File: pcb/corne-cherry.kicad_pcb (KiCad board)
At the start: 2 copper layers, 275.5 x 105.6 mm, 170 parts, among them J1 MJ-4PP-9, J2 OLED, J3 MJ-4PP-9, J4 OLED, J5 Conn_01x01_Male, J6 Conn_01x01_Male, P1 Conn_01x03, P3 Conn_01x03, SW1 SW_PUSH, SW10 SW_PUSH, SW11 SW_PUSH, SW12 SW_PUSH, SW13 SW_PUSH, SW14 SW_PUSH, SW15 SW_PUSH, SW16 SW_PUSH, SW17 SW_PUSH, SW18 SW_PUSH, SW19 SW_PUSH, SW2 SW_PUSH, SW20 SW_PUSH, SW21 SW_PUSH, SW22 SW_PUSH, SW23 SW_PUSH, SW24 SW_PUSH, SW25 SW_PUSH, SW26 SW_PUSH, SW27 SW_PUSH, SW28 SW_PUSH, SW29 SW_PUSH, SW3 SW_PUSH, SW30 SW_PUSH, SW31 SW_PUSH, SW32 SW_PUSH, SW33 SW_PUSH, SW34 SW_PUSH, SW35 SW_PUSH, SW36 SW_PUSH, SW37 SW_PUSH, SW38 SW_PUSH, SW39 SW_PUSH, SW4 SW_PUSH, SW40 SW_PUSH, SW41 SW_PUSH, SW42 SW_PUSH, SW43 Rotary_Encoder_Switch, SW44 Rotary_Encoder_Switch, SW5 SW_PUSH, SW6 SW_PUSH, SW7 SW_PUSH, SW8 SW_PUSH, SW9 SW_PUSH, U1 ProMicro, U2 ProMicro

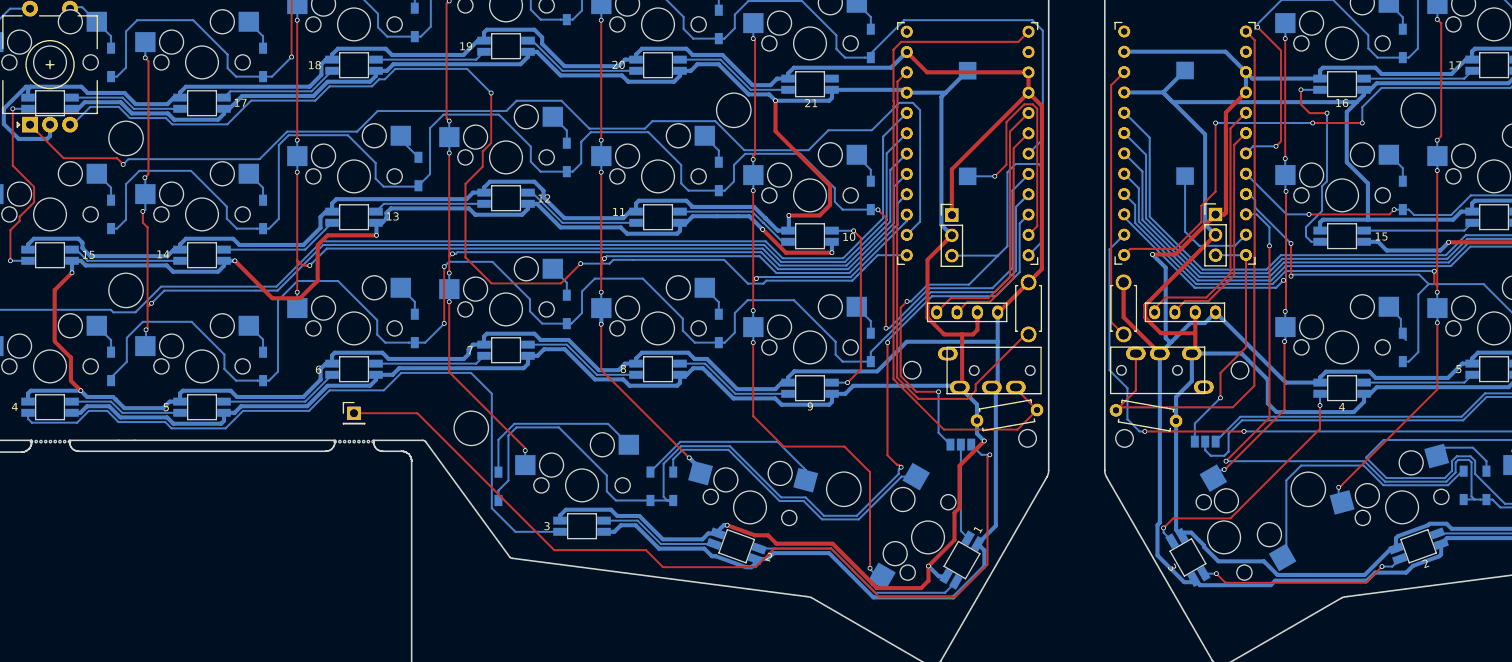
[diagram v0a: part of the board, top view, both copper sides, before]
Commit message: added pimoroni
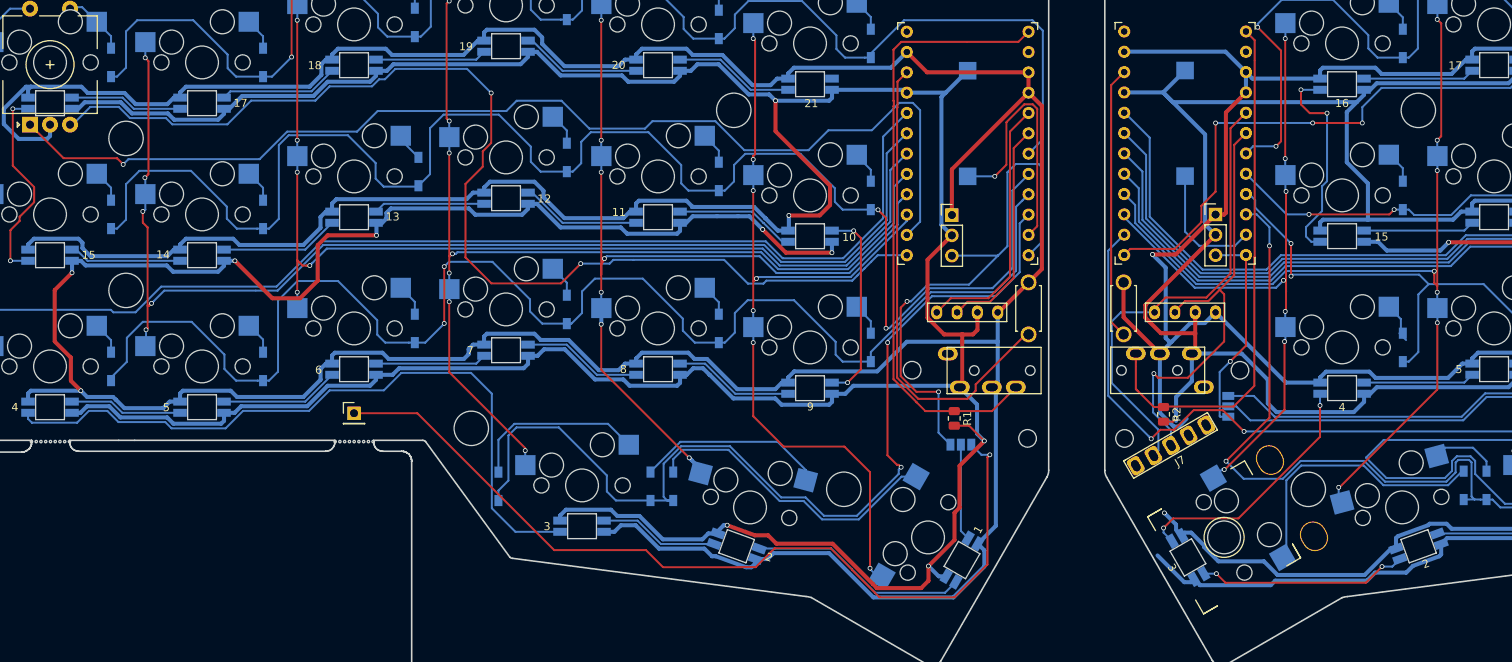
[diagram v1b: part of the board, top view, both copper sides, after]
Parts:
- added J7: Conn_01x05, other_parts:pimoroni-trackballl-bommod, F.Cu at (166.9, 95.2)
- R1, R2: footprint Resistor_THT:R_Axial_DIN0207_L6.3mm_D2.5mm_P7.62mm_Horizontal -> Resistor_SMD:R_0805_2012Metric
- moved R1 10.4 mm to (133.1, 80.3), turned to 270 degrees
- moved R2 5.96 mm to (159.3, 79.8), turned to 270 degrees
- moved JP2 5.27 mm to (167.4, 78.8), turned to 90 degrees
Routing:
- net SCL_r: track 27.9 -> 55.4 mm, vias 0 -> 1
- net SDA_r: track 32.7 -> 58.0 mm
- net GNDA: track 564.7 -> 551.3 mm
- net VDD: track 536.0 -> 527.3 mm, vias 0 -> 2
- net data: track 84.6 -> 77.5 mm
- net Net-(JP2-Pad2): track 76.6 -> 70.0 mm
- net data_r: track 72.5 -> 67.3 mm
- net VCC: track 512.9 -> 517.5 mm
- net LED_r: track 29.8 -> 26.4 mm
- net ENC_A_R: track 257.1 -> 259.9 mm
- net row3_r: track 95.3 -> 97.1 mm
- net Net-(J6-Pad1): track 78.9 -> 77.1 mm
- net (no net): track 1.55 -> 0.00 mm
- net Net-(LED24-Pad4): track 31.2 -> 31.7 mm
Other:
- net class power added: clearance 0.2, trace_width 0.5, via_dia 0.6, via_drill 0.4

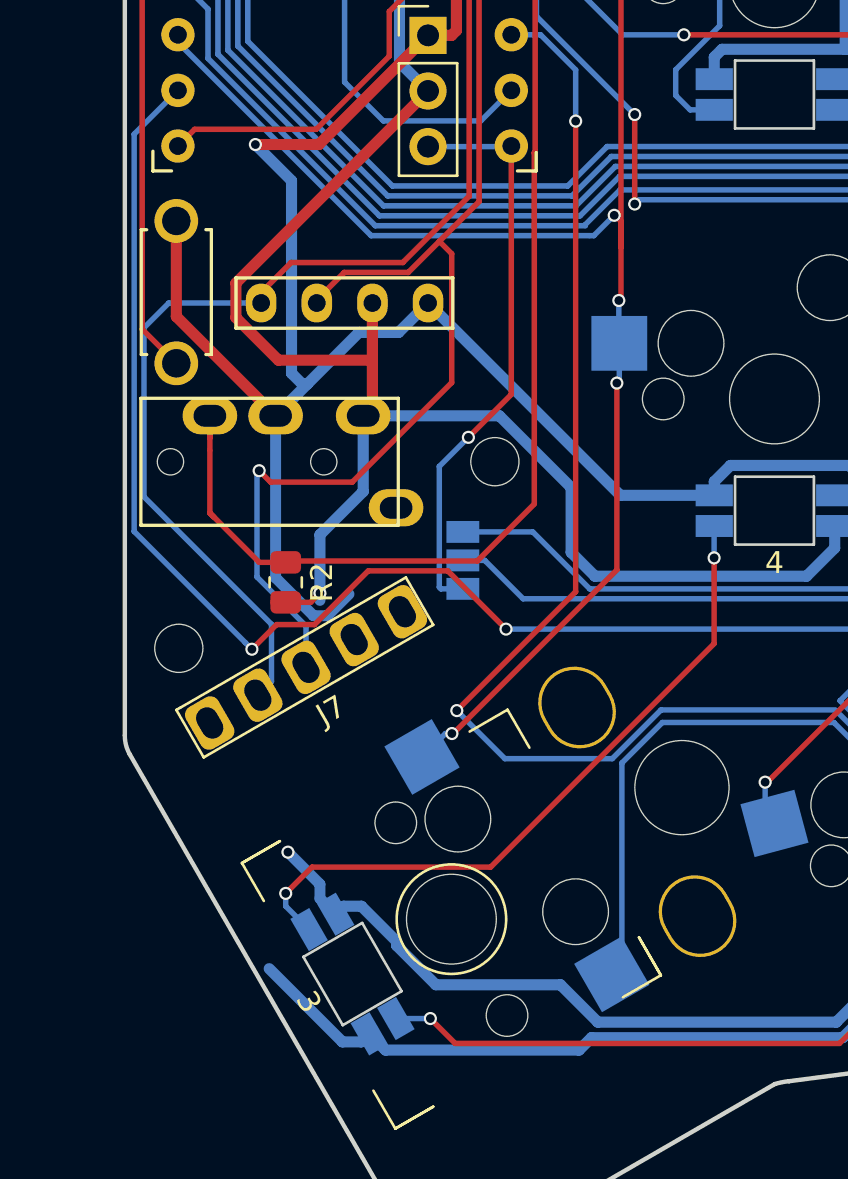
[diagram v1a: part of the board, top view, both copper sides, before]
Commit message: added support for the pimoroni trackball and replotted the gerbers
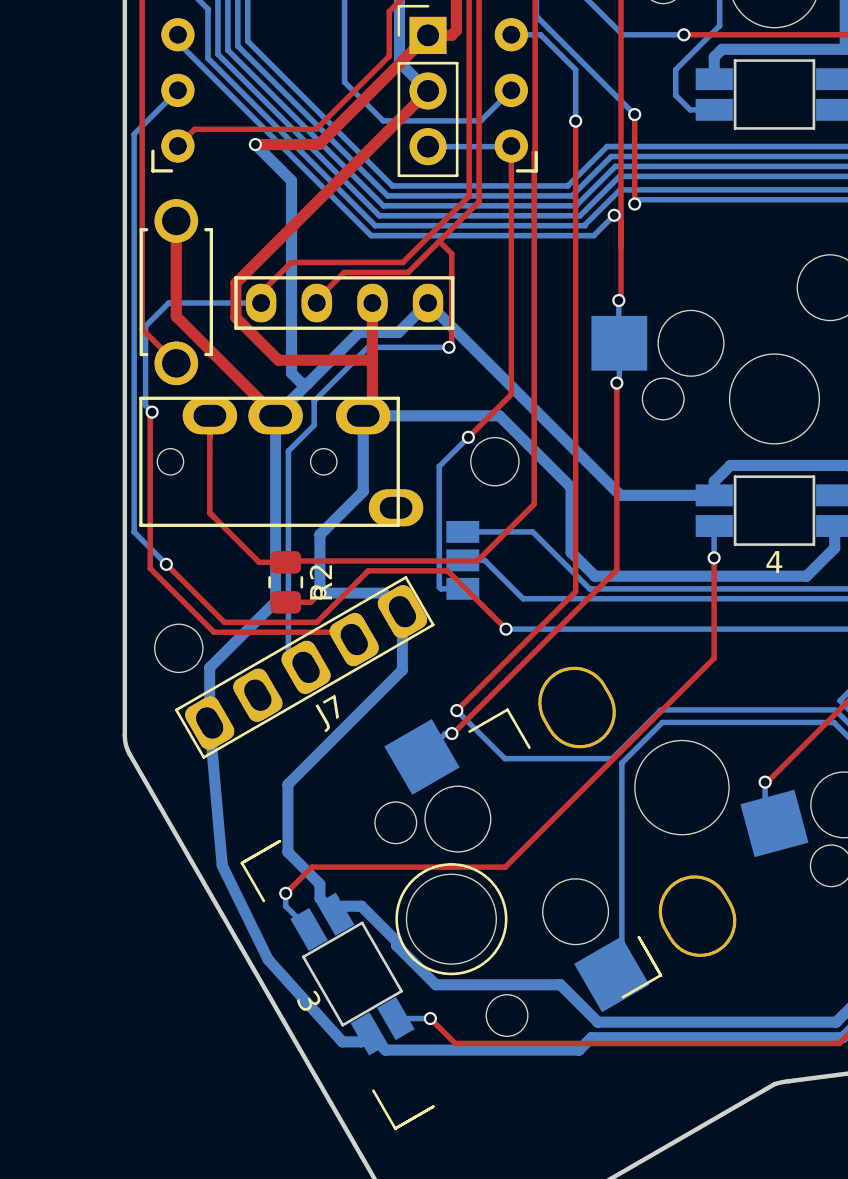
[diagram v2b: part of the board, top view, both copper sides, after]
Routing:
- net VDD: track 527.3 -> 544.2 mm, vias 2 -> 1
- net GNDA: track 551.3 -> 566.3 mm
- net SDA_r: track 58.0 -> 60.3 mm, vias 0 -> 1
- net SCL_r: track 55.4 -> 53.1 mm
- net ENC_A_R: track 259.9 -> 258.9 mm
